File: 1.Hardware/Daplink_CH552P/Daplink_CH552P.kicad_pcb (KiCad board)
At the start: 4 copper layers, 25.3 x 14.2 mm, 19 parts, among them J1 Conn_02x05_Counter_Clockwise, J2 USB_C_Receptacle_USB2.0, SW1 SW_Push, U1 SN74LVC1T45DBV, U2 SN74LVC1T45DBV, U3 CH552G, U4 XC6206P332MR

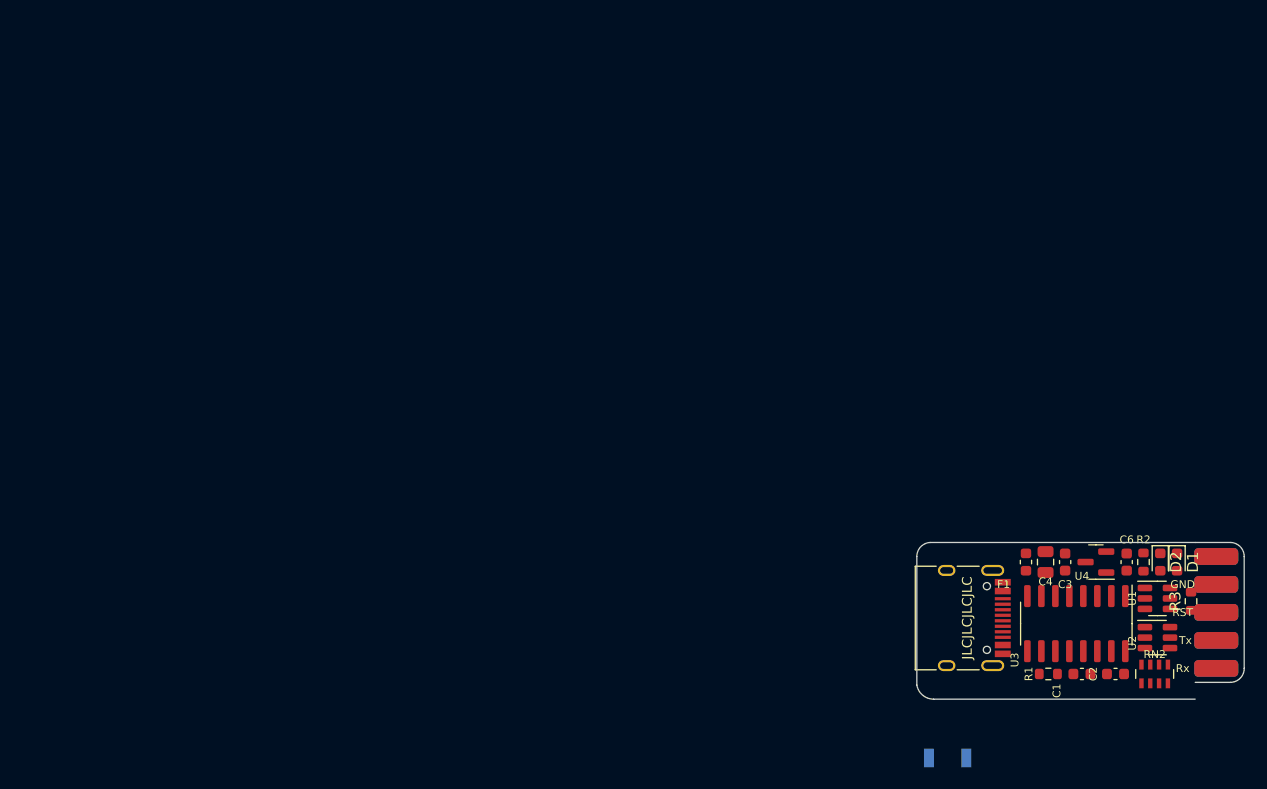
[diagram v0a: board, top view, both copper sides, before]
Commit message: 更新调试器硬件（未测试）
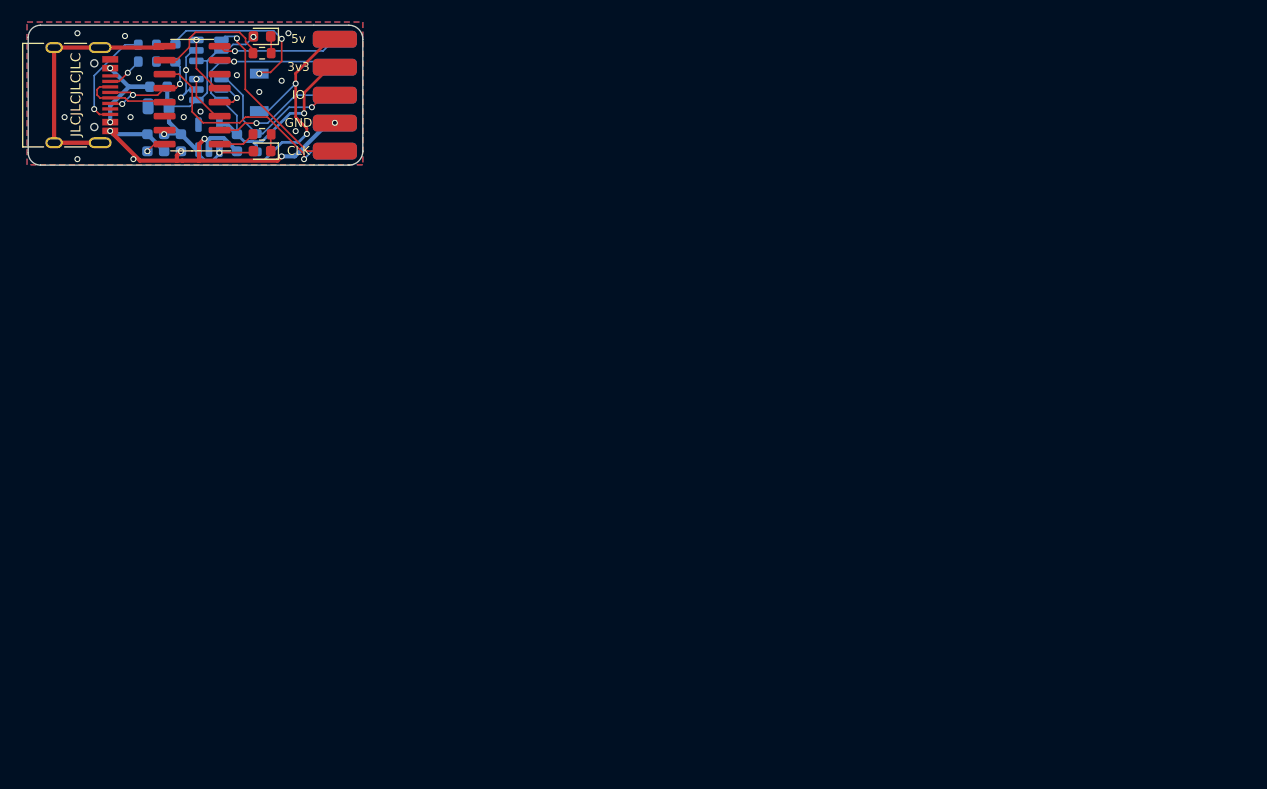
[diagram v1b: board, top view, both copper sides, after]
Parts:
- removed C6: 105, Capacitor_SMD:C_0603_1608Metric
- removed RN2: 5.1K, Resistor_SMD:R_Array_Concave_4x0603
- added C5: 105, Capacitor_SMD:C_0603_1608Metric, B.Cu at (60.7, 41.2)
- added R4: 1k, Resistor_SMD:R_0603_1608Metric, B.Cu at (55.1, 33.1)
- added R5: 5.1k, Resistor_SMD:R_0603_1608Metric, B.Cu at (52.6, 32.3)
- added R6: 5.1k, Resistor_SMD:R_0603_1608Metric, B.Cu at (52.6, 33.8)
- C1, C2, C3, C4, F1, R3, U1, U2: moved to B.Cu
- J1: footprint KiCad库:Connector_2.54mm_2_5P_SMD -> Daplink_Library:Connector_2.54mm_2_5P_SMD; moved to B.Cu
- U4: value XC6206P332MR -> ADP7142AUJZ-5.0; footprint Package_TO_SOT_SMD:SOT-23 -> Package_TO_SOT_SMD:TSOT-23-5; moved to B.Cu
- moved U2 101.3 mm to (58.2, 32.8)
- moved C2 100.2 mm to (52.6, 41.2), turned to -90 degrees
- moved U1 97.7 mm to (58.2, 36.4)
- moved C1 96.3 mm to (54.1, 41.2), turned to -90 degrees
- moved R3 94.5 mm to (62.5, 41.2), turned to -90 degrees
- moved D2 94.5 mm to (63.0, 31.5), turned to 180 degrees
- moved J2 93.9 mm to (45.2, 36.9)
- moved U3 93.5 mm to (56.6, 36.9), turned to 180 degrees
- moved J1 92.8 mm to (69.6, 36.9), turned to 90 degrees
- moved R2 92.4 mm to (63.0, 33.1), turned to 0 degrees
- moved D1 91.1 mm to (63.0, 41.9), turned to 180 degrees
- moved C4 90.5 mm to (53.6, 37.9), turned to 180 degrees
- moved F1 89.8 mm to (53.6, 36.1), turned to 0 degrees
- moved U4 89.3 mm to (58.2, 40.7), turned to 90 degrees
- moved C3 88.8 mm to (55.6, 41.2), turned to -90 degrees
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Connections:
- C3 pad 1: GND -> +5V
- C3 pad 2: +5V -> GND
- J1 pad 1: unconnected-(J1-Pad1) -> /Useless
- R1 pad 2: Net-(U3-Pad10) -> Net-(R1-Pad2)
- R2 pad 1: Net-(U3-Pad9) -> Net-(R2-Pad1)
- SW1 pad 1: GND -> +5V
- U3 pad 1: /SWDIO_DIR -> Net-(R1-Pad2)
- U3 pad 10: Net-(U3-Pad10) -> Net-(R2-Pad1)
- U3 pad 11: /KEY_CAP -> /Useless
- U3 pad 4: /SWDIO_5 -> /SWDIO_DIR
- U3 pad 9: Net-(U3-Pad9) -> /KEY_CAP
- U4 pad 1: GND -> +5V
- U4 pad 2: +3V3 -> GND
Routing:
- net +5V: track 0.00 -> 54.5 mm, vias 0 -> 5
- net GND: track 0.00 -> 43.7 mm, vias 0 -> 21
- net +3V3: track 0.00 -> 25.0 mm, vias 0 -> 1
- net /KEY_CAP: track 0.00 -> 22.9 mm
- net /Useless: track 0.00 -> 21.0 mm, vias 0 -> 1
- net /SWCLK: track 0.00 -> 17.0 mm, vias 0 -> 1
- net Net-(R4-Pad1): track 0.00 -> 15.1 mm, vias 0 -> 2
- net /SWDIO: track 0.00 -> 15.1 mm, vias 0 -> 1
- net /nRST: track 0.00 -> 11.8 mm, vias 0 -> 1
- net /USB_DP: track 0.00 -> 11.4 mm, vias 0 -> 3
- net /U_Rx: track 0.00 -> 11.1 mm, vias 0 -> 1
- net Net-(R2-Pad1): track 0.00 -> 10.7 mm
- net /U_Tx: track 0.00 -> 10.7 mm, vias 0 -> 1
- net Net-(F1-Pad1): track 0.00 -> 10.1 mm, vias 0 -> 2
- net Net-(J2-PadB5): track 0.00 -> 9.86 mm, vias 0 -> 1
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- added copper zone on B.Cu, net GND
- added copper zone on F.Cu, net GND
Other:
- board size 25.3 x 14.2 mm -> 25.9 x 12.7 mm
- copper layers 4 -> 2
- board text added: "GitHub: abgelehnt Tiny-DAPLink"
- board text added: "Usr"

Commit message: 更新硬件（未测试）
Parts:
- U4: value ADP7142AUJZ-5.0 -> RT9193-33GB
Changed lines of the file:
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@@
       (effects (font (size 1 1) (thickness 0.15)) (justify mirror))
     )
-    (fp_text value "ADP7142AUJZ-5.0" (at 0 -2.4 90) (layer "B.Fab")
+    (fp_text value "RT9193-33GB" (at 0 -2.4 90) (layer "B.Fab")
       (effects (font (size 1 1) (thickness 0.15)) (justify mirror))
     )
